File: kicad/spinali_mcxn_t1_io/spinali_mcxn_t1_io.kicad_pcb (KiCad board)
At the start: 4 copper layers, 36.5 x 46 mm, 76 parts, among them J1 DF40TC(4.0)-50DS-0.4V(51), J10 SPI2, J11 ESC1, J12 ESC2, J13 RTC_BAT, J2 DF40TC(4.0)-50DS-0.4V(51), J3 I2C1, J4 I2C2, J5 UART1, J6 UART2, J7 QDEC, J8 GPS, J9 SPI1, Q1 NX138BKMYL, SW1 CHS-01TA

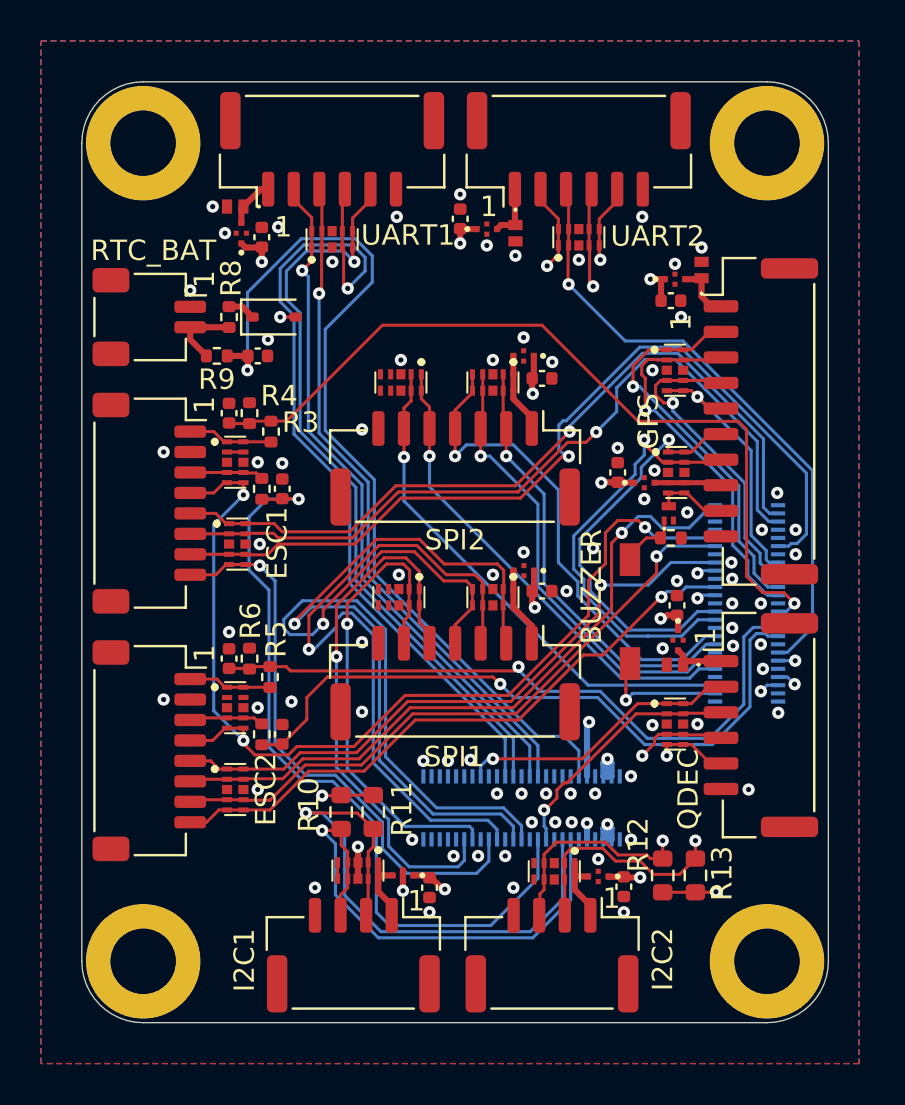
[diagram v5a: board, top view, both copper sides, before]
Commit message: Updated schematic and layout after review (ready for production)
- Replaced TVS diode at ESC1 and ESC2 connector with higher voltage one.
- Replaced MUTAG7104 TVS with single TVS at some places to reduce cost.
- Added 1k5 pull-down resistor on GPS safety switch.
- Generated all production files.
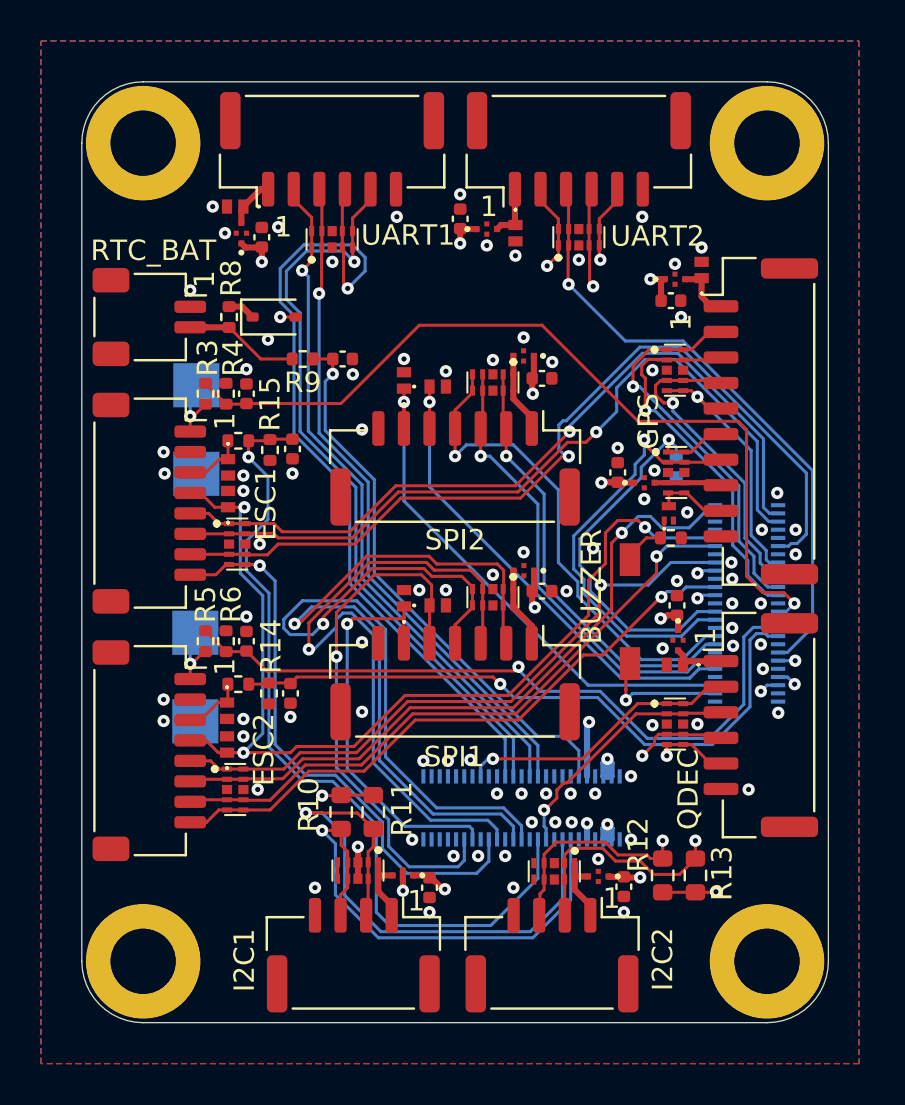
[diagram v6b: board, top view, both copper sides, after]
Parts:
- added D20: P6SMB62A, TVS:SOD1002-1, B.Cu at (122.6, 69.0)
- added D21: P6SMB62A, TVS:SOD1002-1, B.Cu at (122.5, 81.1)
- added D22: PESD5V0S1UL, TVS:PESD5V0S1ULD315, F.Cu at (124.2, 70.8)
- added D23: PESD5V0S1UL, TVS:PESD5V0S1ULD315, F.Cu at (124.2, 72.4)
- added D25: PESD5V0S1UL, TVS:PESD5V0S1ULD315, F.Cu at (134.4, 77.6)
- added D26: PESD5V0S1UL, TVS:PESD5V0S1ULD315, F.Cu at (132.8, 77.2)
- added R14: 10R, Resistor_SMD:R_0402_1005Metric, F.Cu at (126.2, 81.9)
- added R15: 10R, Resistor_SMD:R_0402_1005Metric, F.Cu at (126.2, 70.0)
- added R16: 1k5, Resistor_SMD:R_0402_1005Metric, B.Cu at (146.1, 70.8)
- D16, D18, D4, D6: value ESD7104MUTAG -> PESD5V0S1UL; footprint TVS:ESD8104MUTAG -> TVS:PESD5V0S1ULD315
- moved D16 12.2 mm to (124.1, 82.8)
- moved D4 10.6 mm to (132.8, 66.6), turned to 90 degrees
- moved R9 4.20 mm to (127.8, 65.5)
- moved C23 4.15 mm to (129.8, 65.5)
- moved R3 3.70 mm to (123.0, 67.2)
- moved R5 3.60 mm to (123.0, 79.3)
- moved R2 2.71 mm to (124.7, 81.5), turned to 180 degrees
- moved R1 2.62 mm to (124.7, 69.5), turned to 180 degrees
- moved C21 2.04 mm to (127.2, 81.9)
- moved C19 2.01 mm to (127.3, 70.0)
- moved D18 1.84 mm to (124.1, 84.4), turned to 90 degrees
- moved D6 1.81 mm to (134.4, 66.9), turned to 0 degrees
- moved R4 1.49 mm to (124.0, 67.2)
- moved R6 1.43 mm to (124.0, 79.3)
- moved C20 1.27 mm to (125.0, 67.2)
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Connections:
- C19 pad 1: P1_23/ADC1_A23 -> GND
- C19 pad 2: GND -> P1_23/ADC1_A23
- C21 pad 1: P1_17/ADC1_A17 -> GND
- C21 pad 2: GND -> P1_17/ADC1_A17
- D16 pad 1: /IO2/VBAT1 -> /IO2/CURR2
- D16 pad 2: unconnected-(D16-IO_2-Pad2) -> GND
- D18 pad 1: /IO2/VBAT2 -> P2_3/FC9_P1_UART_TXD
- D18 pad 2: unconnected-(D18-IO_2-Pad2) -> GND
- D4 pad 1: P3_13/FC6_P5_SPI_CS2 -> P3_19/FC7_P6_SPI_HREQ
- D4 pad 2: P3_18/FC6_P6_SPI_HREQ -> GND
- D6 pad 2: P3_19/FC7_P6_SPI_HREQ -> GND
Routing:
- net VDD_BAT: track 45.4 -> 27.4 mm
- net P3_18/FC6_P6_SPI_HREQ: track 23.6 -> 19.7 mm
- net P1_23/ADC1_A23: track 38.4 -> 40.6 mm
- net Net-(J13-1-Pad2): track 3.63 -> 5.63 mm
- net P1_16/ADC1_A16: track 32.8 -> 34.7 mm
- net P3_5/FC7_P3_SPI_CS0: track 23.7 -> 25.5 mm
- net P2_3/FC9_P1_UART_TXD: track 50.5 -> 48.7 mm
- net P3_19/FC7_P6_SPI_HREQ: track 25.3 -> 27.0 mm
- net P1_17/ADC1_A17: track 32.8 -> 31.6 mm
- net P1_18/ADC1_A18: track 40.5 -> 41.6 mm
- net P2_9/SAFETY_SW: track 20.2 -> 21.2 mm
- net P3_1/FC6_P0_SPI_SDO: track 36.6 -> 35.7 mm
- net P3_10/FC6_P2_SPI_SDI: track 34.0 -> 33.1 mm
- net P3_13/FC6_P5_SPI_CS2: track 27.1 -> 26.3 mm
- net unconnected-(D16-IO_2-Pad2): track 0.80 -> 0.00 mm
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
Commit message: Updated MCXN-T1 IO board
- Fixed that JST GH connectors are now the correct part number.
- Updated silkscreen positioning.
- Generated production files for Eurocircuits (global) and JLCPCB
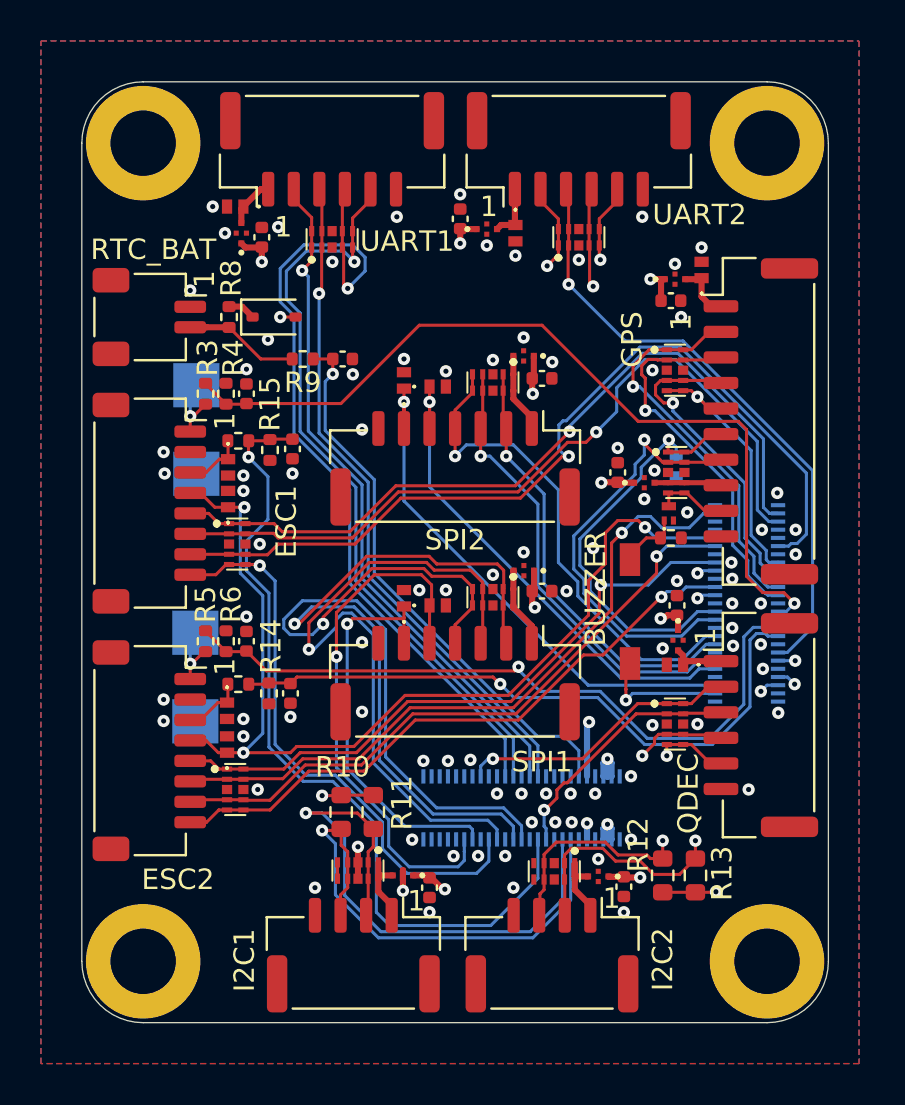
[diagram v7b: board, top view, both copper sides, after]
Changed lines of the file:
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@@
 		)
 		(property "Value" "UART1"
-			(at 3.7125 4.2 180)
+			(at 3.6625 4.5 180)
 			(layer "F.SilkS")
 			(effects
@@
 			)
 		)
-		(property "MFPN" "SM06B-GHS-TB"
+		(property "MFPN" "BM06B-GHS-TBT"
 			(at 0 0 0)
 			(unlocked yes)
@@
 			)
 		)
-		(property "DigiKey" "455-1568-1-ND"
+		(property "DigiKey" "455-BM06B-GHS-TBTCT-ND"
 			(at 0 0 0)
 			(unlocked yes)
@@
 		)
 		(property "Value" "QDEC"
-			(at 3.15 3.55 90)
+			(at 3.35 3.55 90)
 			(layer "F.SilkS")
 			(effects
@@
 			)
 		)
-		(property "MFPN" "SM06B-GHS-TB"
+		(property "MFPN" "BM06B-GHS-TBT"
 			(at 0 0 270)
 			(unlocked yes)
@@
 			)
 		)
-		(property "DigiKey" "455-1568-1-ND"
+		(property "DigiKey" "455-BM06B-GHS-TBTCT-ND"
 			(at 0 0 270)
 			(unlocked yes)
@@
 		)
 		(property "Value" "UART2"
-			(at 3.85 4.25 0)
+			(at 5.9 3.2 0)
 			(layer "F.SilkS")
 			(effects
@@
 			)
 		)
-		(property "MFPN" "SM06B-GHS-TB"
+		(property "MFPN" "BM06B-GHS-TBT"
 			(at 0 0 0)
 			(unlocked yes)
@@
 			)
 		)
-		(property "DigiKey" "455-1568-1-ND"
+		(property "DigiKey" "455-BM06B-GHS-TBTCT-ND"
 			(at 0 0 0)
 			(unlocked yes)
@@
 		(tags "resistor")
 		(property "Reference" "R11"
-			(at -0.15 -1.4 90)
+			(at -0.45 -1.4 90)
 			(layer "F.SilkS")
 			(effects
@@
 		)
 		(property "Value" "ESC1"
-			(at 0.05 -5.7 90)
+			(at 0.9 -6.7 90)
 			(layer "F.SilkS")
 			(effects
@@
 		)
 		(property "Value" "RTC_BAT"
-			(at -3.25 -0.2 180)
+			(at -3.3 -0.2 180)
 			(layer "F.SilkS")
 			(effects
@@
 			)
 		)
-		(property "MFPN" "SM04B-GHS-TB"
+		(property "MFPN" "BM04B-GHS-TBT"
 			(at 0 0 180)
 			(unlocked yes)
@@
 			)
 		)
-		(property "DigiKey" "455-1566-1-ND"
+		(property "DigiKey" "455-BM04B-GHS-TBTCT-ND"
 			(at 0 0 180)
 			(unlocked yes)
@@
 			)
 		)
-		(property "MFPN" "SM07B-GHS-TB"
+		(property "MFPN" "BM07B-GHS-TBT"
 			(at 0 0 0)
 			(unlocked yes)
@@
 			)
 		)
-		(property "DigiKey" "455-1569-1-ND"
+		(property "DigiKey" "455-BM07B-GHS-TBTCT-ND"
 			(at 0 0 0)
 			(unlocked yes)
@@
 		)
 		(property "Value" "ESC2"
-			(at -0.05 -5.6 90)
+			(at 6.3 -1.4 180)
 			(layer "F.SilkS")
 			(effects
@@
 		)
 		(property "Value" "SPI1"
-			(at 0.05 -3.6 0)
+			(at -4.25 -3.85 0)
 			(layer "F.SilkS")
 			(effects
@@
 			)
 		)
-		(property "MFPN" "SM07B-GHS-TB"
+		(property "MFPN" "BM07B-GHS-TBT"
 			(at 0 0 180)
 			(unlocked yes)
@@
 			)
 		)
-		(property "DigiKey" "455-1569-1-ND"
+		(property "DigiKey" "455-BM07B-GHS-TBTCT-ND"
 			(at 0 0 180)
 			(unlocked yes)
@@
 		)
 		(property "Value" "GPS"
-			(at 0 5.5 90)
+			(at -4 6.3 90)
 			(layer "F.SilkS")
 			(effects
@@
 			)
 		)
-		(property "MFPN" "SM10B-GHS-TB"
+		(property "MFPN" "BM10B-GHS-TBT"
 			(at 0 0 270)
 			(unlocked yes)
@@
 			)
 		)
-		(property "DigiKey" "455-SM10B-GHS-TBCT-ND"
+		(property "DigiKey" "455-BM10B-GHS-TBTCT-ND"
 			(at 0 0 270)
 			(unlocked yes)
@@
 			)
 		)
-		(property "MFPN" "SM04B-GHS-TB"
+		(property "MFPN" "BM04B-GHS-TBT"
 			(at 0 0 180)
 			(unlocked yes)
@@
 			)
 		)
-		(property "DigiKey" "455-1566-1-ND"
+		(property "DigiKey" "455-BM04B-GHS-TBTCT-ND"
 			(at 0 0 180)
 			(unlocked yes)
@@
 		(tags "resistor")
 		(property "Reference" "R10"
-			(at -0.35 1.58 90)
+			(at -2.2 -0.07 180)
 			(layer "F.SilkS")
 			(effects
@@
 	)
 	(gr_text "BUZZER"
-		(at 142.5 79.5 90)
+		(at 142.7 79.6 90)
 		(layer "F.SilkS")
 		(effects
@@
 			(clearance 0.1)
 		)
-		(min_thickness 0.1)
+		(min_thickness 0.15)
 		(filled_areas_thickness no)
 		(fill yes
@@
 			(clearance 0.1)
 		)
-		(min_thickness 0.1)
+		(min_thickness 0.15)
 		(filled_areas_thickness no)
 		(fill yes
